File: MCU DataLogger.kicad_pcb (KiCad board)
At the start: 2 copper layers, 29 parts, among them J1 Conn_01x04_Male, J2 Conn_01x04_Male, J3 Conn_01x09_Male, J4 Conn_02x03_Odd_Even, U1 24LC1025, U2 24LC1025, U3 DS1337S+, U4 ATMEGA328P-AU, Y1 32.768 KHz, Y2 16 MHz

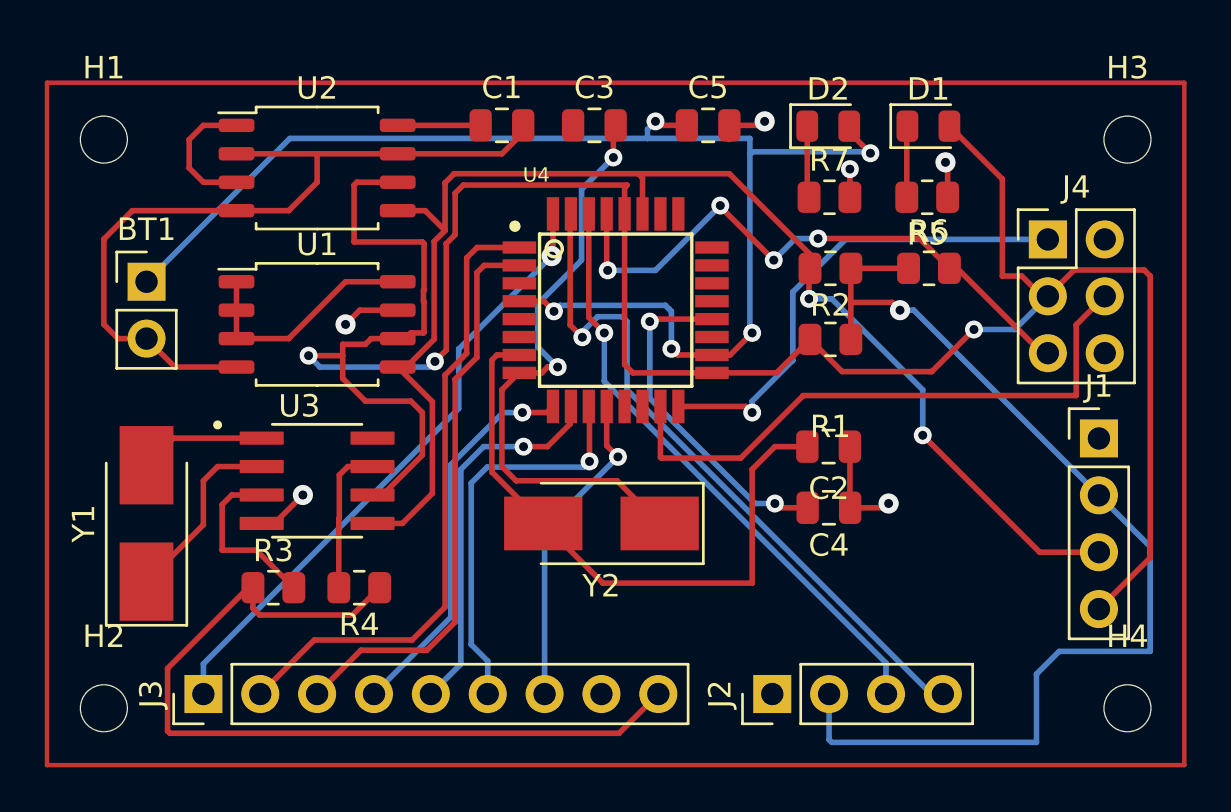
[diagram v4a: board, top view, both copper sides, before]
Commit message: Add Cu surface 1/2
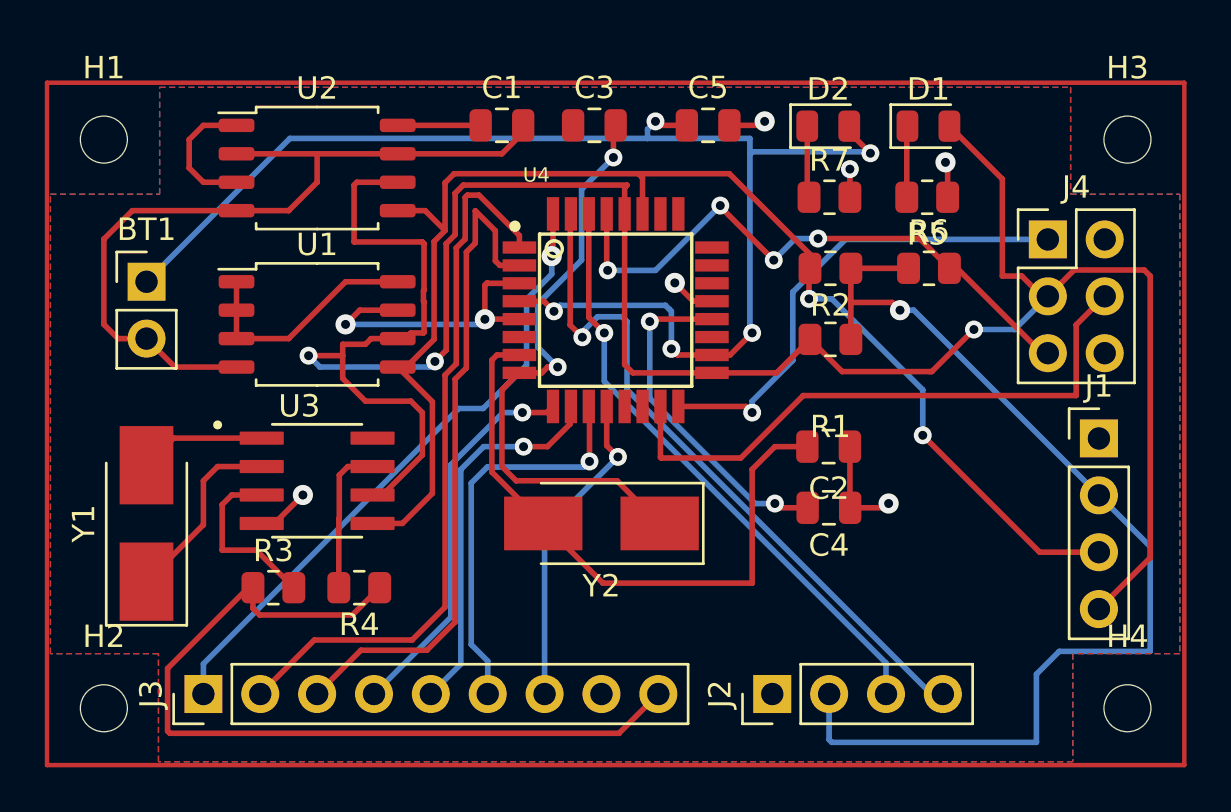
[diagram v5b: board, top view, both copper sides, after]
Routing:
- net GND: track 50.5 -> 62.9 mm, vias 6 -> 8
- net /D4: track 25.5 -> 30.0 mm
- net /D3: track 28.4 -> 32.3 mm
- net /D2: track 27.9 -> 28.6 mm
- added copper zone on F.Cu, net /Vcc
- added copper zone on B.Cu, net GND
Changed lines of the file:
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@@
   (segment (start 75.502 102.806) (end 75.692 102.616) (width 0.25) (layer "F.Cu") (net 2))
   (segment (start 42.545 95.25) (end 43.815 96.52) (width 0.25) (layer "F.Cu") (net 2))
+  (segment (start 57.7596 92.7608) (end 57.7788 92.78) (width 0.25) (layer "F.Cu") (net 2))
+  (segment (start 67.8 93.58) (end 66.9608 93.58) (width 0.25) (layer "F.Cu") (net 2))
   (segment (start 69.977 85.725) (end 70.1548 85.5472) (width 0.25) (layer "F.Cu") (net 2))
-  (segment (start 68.58 85.725) (end 68.58 86.36) (width 0.25) (layer "F.Cu") (net 2))
+  (segment (start 57.6644 94.38) (end 57.658 94.3864) (width 0.25) (layer "F.Cu") (net 2))
   (segment (start 78.3275 87.4715) (end 78.232 87.376) (width 0.25) (layer "F.Cu") (net 2))
   (segment (start 59.37 86.045) (end 58.42 86.995) (width 0.25) (layer "F.Cu") (net 2))
   (segment (start 47.69 103.505) (end 48.26 103.505) (width 0.25) (layer "F.Cu") (net 2))
+  (segment (start 57.658 94.3864) (end 57.658 92.8624) (width 0.25) (layer "F.Cu") (net 2))
   (segment (start 40.64 90.805) (end 41.91 89.535) (width 0.25) (layer "F.Cu") (net 2))
   (segment (start 46.565 86.995) (end 50.165 86.995) (width 0.25) (layer "F.Cu") (net 2))
+  (segment (start 57.658 92.8624) (end 57.7596 92.7608) (width 0.25) (layer "F.Cu") (net 2))
   (segment (start 73.9625 87.6785) (end 73.9625 88.935) (width 0.25) (layer "F.Cu") (net 2))
   (segment (start 46.565 89.535) (end 48.895 89.535) (width 0.25) (layer "F.Cu") (net 2))
@@
   (segment (start 42.545 95.25) (end 41.275 95.25) (width 0.25) (layer "F.Cu") (net 2))
   (segment (start 41.275 95.25) (end 40.64 94.615) (width 0.25) (layer "F.Cu") (net 2))
+  (segment (start 66.9608 93.58) (end 66.1416 92.7608) (width 0.25) (layer "F.Cu") (net 2))
   (segment (start 41.91 89.535) (end 46.565 89.535) (width 0.25) (layer "F.Cu") (net 2))
   (segment (start 68.58 85.725) (end 69.977 85.725) (width 0.25) (layer "F.Cu") (net 2))
@@
   (segment (start 59.37 85.725) (end 59.37 86.045) (width 0.25) (layer "F.Cu") (net 2))
   (segment (start 40.64 94.615) (end 40.64 90.805) (width 0.25) (layer "F.Cu") (net 2))
+  (segment (start 57.7788 92.78) (end 59.2 92.78) (width 0.25) (layer "F.Cu") (net 2))
+  (segment (start 59.2 94.38) (end 57.6644 94.38) (width 0.25) (layer "F.Cu") (net 2))
   (segment (start 52.07 93.98) (end 51.435 94.615) (width 0.25) (layer "F.Cu") (net 2))
   (segment (start 43.815 96.52) (end 46.565 96.52) (width 0.25) (layer "F.Cu") (net 2))
@@
   (via (at 75.692 102.616) (size 0.9) (drill 0.4) (layers "F.Cu" "B.Cu") (net 2))
   (via (at 51.435 94.615) (size 0.9) (drill 0.4) (layers "F.Cu" "B.Cu") (net 2))
+  (via (at 66.1416 92.7608) (size 0.9) (drill 0.4) (layers "F.Cu" "B.Cu") (net 2))
+  (via (at 57.658 94.3864) (size 0.9) (drill 0.4) (layers "F.Cu" "B.Cu") (net 2))
+  (segment (start 57.658 94.3864) (end 57.4294 94.615) (width 0.25) (layer "B.Cu") (net 2))
+  (segment (start 57.4294 94.615) (end 51.435 94.615) (width 0.25) (layer "B.Cu") (net 2))
   (segment (start 60.9092 96.52) (end 60.46 96.52) (width 0.25) (layer "F.Cu") (net 3))
   (segment (start 63.56 101.6) (end 59.055 101.6) (width 0.25) (layer "F.Cu") (net 3))
@@
   (segment (start 60.7 91.507736) (end 60.7 89.68) (width 0.25) (layer "F.Cu") (net 11))
   (via (at 60.6435 91.564236) (size 0.9) (drill 0.4) (layers "F.Cu" "B.Cu") (net 11))
-  (segment (start 60.6435 91.564236) (end 56.4896 95.718136) (width 0.25) (layer "B.Cu") (net 11))
+  (segment (start 60.6435 91.564236) (end 60.6435 92.370194) (width 0.25) (layer "B.Cu") (net 11))
+  (segment (start 57.585616 98.370384) (end 56.4896 98.370384) (width 0.25) (layer "B.Cu") (net 11))
+  (segment (start 56.4896 98.370384) (end 45.085 109.774984) (width 0.25) (layer "B.Cu") (net 11))
+  (segment (start 59.5185 93.495194) (end 59.5185 96.4375) (width 0.25) (layer "B.Cu") (net 11))
+  (segment (start 60.6435 92.370194) (end 59.5185 93.495194) (width 0.25) (layer "B.Cu") (net 11))
   (segment (start 45.085 109.774984) (end 45.085 111.125) (width 0.25) (layer "B.Cu") (net 11))
-  (segment (start 56.4896 95.718136) (end 56.4896 98.370384) (width 0.25) (layer "B.Cu") (net 11))
-  (segment (start 56.4896 98.370384) (end 45.085 109.774984) (width 0.25) (layer "B.Cu") (net 11))
+  (segment (start 59.5185 96.4375) (end 57.585616 98.370384) (width 0.25) (layer "B.Cu") (net 11))
+  (segment (start 56.78 90.796792) (end 56.3808 91.195992) (width 0.25) (layer "F.Cu") (net 12))
+  (segment (start 56.78 88.941196) (end 56.78 90.796792) (width 0.25) (layer "F.Cu") (net 12))
+  (segment (start 57.3968 88.842) (end 56.879196 88.842) (width 0.25) (layer "F.Cu") (net 12))
+  (segment (start 59.2 91.18) (end 59.2 90.6452) (width 0.25) (layer "F.Cu") (net 12))
+  (segment (start 54.4068 108.712) (end 50.038 108.712) (width 0.25) (layer "F.Cu") (net 12))
+  (segment (start 50.038 108.712) (end 47.625 111.125) (width 0.25) (layer "F.Cu") (net 12))
+  (segment (start 56.879196 88.842) (end 56.78 88.941196) (width 0.25) (layer "F.Cu") (net 12))
+  (segment (start 56.3808 91.195992) (end 56.3808 96.3748) (width 0.25) (layer "F.Cu") (net 12))
   (segment (start 55.88 107.2388) (end 54.4068 108.712) (width 0.25) (layer "F.Cu") (net 12))
-  (segment (start 50.038 108.712) (end 47.625 111.125) (width 0.25) (layer "F.Cu") (net 12))
-  (segment (start 54.4068 108.712) (end 50.038 108.712) (width 0.25) (layer "F.Cu") (net 12))
-  (segment (start 59.2 91.18) (end 57.3084 91.18) (width 0.25) (layer "F.Cu") (net 12))
-  (segment (start 56.8452 95.9104) (end 55.88 96.8756) (width 0.25) (layer "F.Cu") (net 12))
   (segment (start 55.88 96.8756) (end 55.88 107.2388) (width 0.25) (layer "F.Cu") (net 12))
-  (segment (start 56.8452 91.6432) (end 56.8452 95.9104) (width 0.25) (layer "F.Cu") (net 12))
-  (segment (start 57.3084 91.18) (end 56.8452 91.6432) (width 0.25) (layer "F.Cu") (net 12))
+  (segment (start 59.2 90.6452) (end 57.3968 88.842) (width 0.25) (layer "F.Cu") (net 12))
+  (segment (start 56.3808 96.3748) (end 55.88 96.8756) (width 0.25) (layer "F.Cu") (net 12))
+  (segment (start 57.23 89.5388) (end 58.125 90.4338) (width 0.25) (layer "F.Cu") (net 13))
+  (segment (start 58.125 91.78) (end 58.325 91.98) (width 0.25) (layer "F.Cu") (net 13))
+  (segment (start 56.33 107.9064) (end 56.33 97.061996) (width 0.25) (layer "F.Cu") (net 13))
   (segment (start 52.1208 109.1692) (end 55.0672 109.1692) (width 0.25) (layer "F.Cu") (net 13))
   (segment (start 55.0672 109.1692) (end 56.33 107.9064) (width 0.25) (layer "F.Cu") (net 13))
-  (segment (start 57.3024 92.3036) (end 57.626 91.98) (width 0.25) (layer "F.Cu") (net 13))
-  (segment (start 56.33 107.9064) (end 56.33 97.061996) (width 0.25) (layer "F.Cu") (net 13))
-  (segment (start 57.626 91.98) (end 59.2 91.98) (width 0.25) (layer "F.Cu") (net 13))
-  (segment (start 56.33 97.061996) (end 57.3024 96.089596) (width 0.25) (layer "F.Cu") (net 13))
+  (segment (start 57.23 90.983188) (end 57.23 89.5388) (width 0.25) (layer "F.Cu") (net 13))
+  (segment (start 56.33 97.061996) (end 56.8308 96.561196) (width 0.25) (layer "F.Cu") (net 13))
+  (segment (start 56.8308 96.561196) (end 56.8308 91.382388) (width 0.25) (layer "F.Cu") (net 13))
+  (segment (start 58.125 90.4338) (end 58.125 91.78) (width 0.25) (layer "F.Cu") (net 13))
+  (segment (start 58.325 91.98) (end 59.2 91.98) (width 0.25) (layer "F.Cu") (net 13))
   (segment (start 50.165 111.125) (end 52.1208 109.1692) (width 0.25) (layer "F.Cu") (net 13))
-  (segment (start 57.3024 96.089596) (end 57.3024 92.3036) (width 0.25) (layer "F.Cu") (net 13))
+  (segment (start 56.8308 91.382388) (end 57.23 90.983188) (width 0.25) (layer "F.Cu") (net 13))
   (segment (start 59.3344 98.552) (end 60.428 98.552) (width 0.25) (layer "F.Cu") (net 14))
   (segment (start 60.428 98.552) (end 60.7 98.28) (width 0.25) (layer "F.Cu") (net 14))
@@
   (segment (start 70.612 102.616) (end 69.724396 102.616) (width 0.25) (layer "B.Cu") (net 35))
   (segment (start 65.024 97.915604) (end 65.024 94.488) (width 0.25) (layer "B.Cu") (net 35))
+  (zone (net 7) (net_name "/Vcc") (layer "F.Cu") (hatch edge 0.508)
+    (connect_pads (clearance 0.508))
+    (min_thickness 0.254) (filled_areas_thickness no)
+    (fill yes (mode hatch) (thermal_gap 0.508) (thermal_bridge_width 0.508)
+      (hatch_thickness 1.016) (hatch_gap 1.524) (hatch_orientation 0)
+      (hatch_border_algorithm hatch_thickness) (hatch_min_hole_area 0.3))
+    (polygon
+      (pts
+        (xy 83.82 88.7984)
+        (xy 88.6968 88.7984)
+        (xy 88.6968 109.3216)
+        (xy 83.9216 109.3216)
+        (xy 83.9216 114.1476)
+        (xy 43.0784 114.1476)
+        (xy 43.0784 109.3216)
+        (xy 38.2524 109.3216)
+        (xy 38.2524 88.7984)
+        (xy 43.1292 88.7984)
+        (xy 43.1292 84.0232)
+        (xy 83.82 84.0232)
+      )
+    )
+  )
+  (zone (net 2) (net_name "GND") (layer "B.Cu") (hatch edge 0.508)
+    (connect_pads (clearance 0.508))
+    (min_thickness 0.254) (filled_areas_thickness no)
+    (fill yes (mode hatch) (thermal_gap 0.508) (thermal_bridge_width 0.508)
+      (hatch_thickness 1.016) (hatch_gap 1.524) (hatch_orientation 0)
+      (hatch_border_algorithm hatch_thickness) (hatch_min_hole_area 0.3))
+    (polygon
+      (pts
+        (xy 83.82 88.7984)
+        (xy 88.6968 88.7984)
+        (xy 88.6968 109.3216)
+        (xy 83.9216 109.3216)
+        (xy 83.9216 114.1476)
+        (xy 43.0784 114.1476)
+        (xy 43.0784 109.3216)
+        (xy 38.2524 109.3216)
+        (xy 38.2524 88.7984)
+        (xy 43.1292 88.7984)
+        (xy 43.1292 84.0232)
+        (xy 83.82 84.0232)
+      )
+    )
+  )
 )

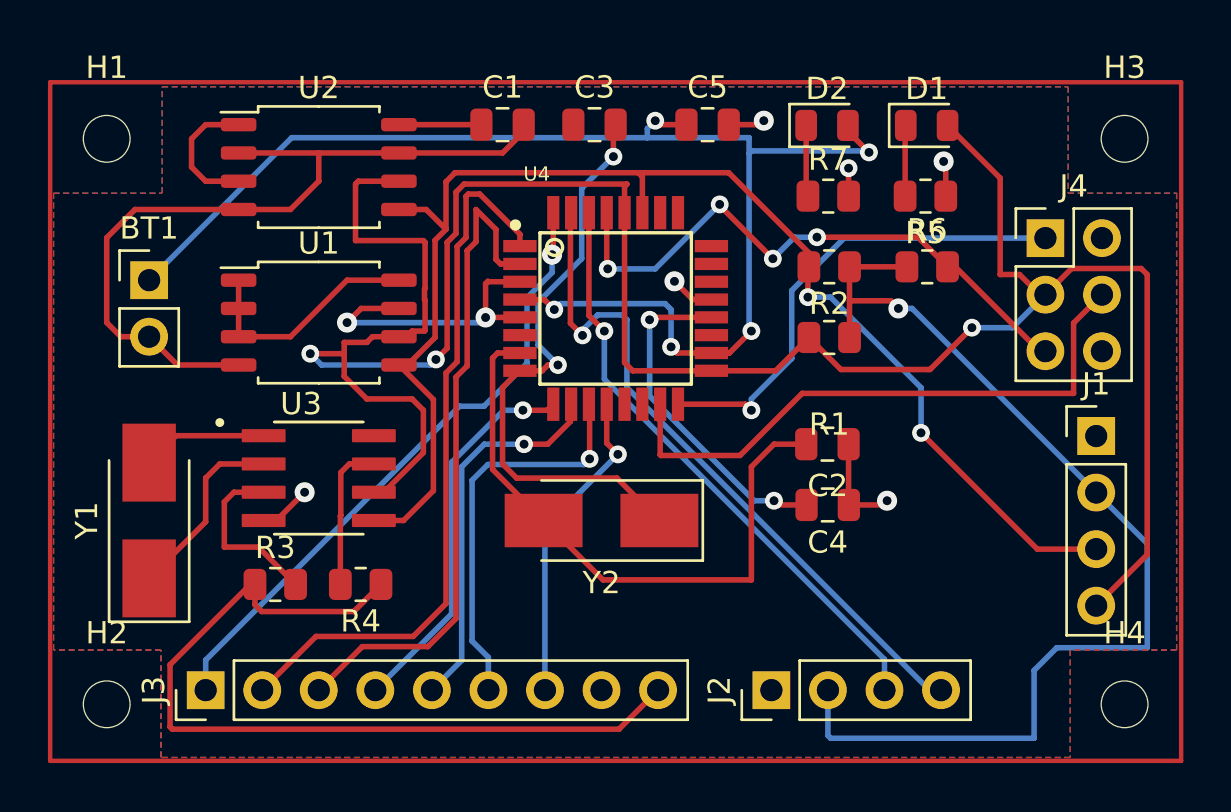
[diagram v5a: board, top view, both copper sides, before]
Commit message: Completed routing
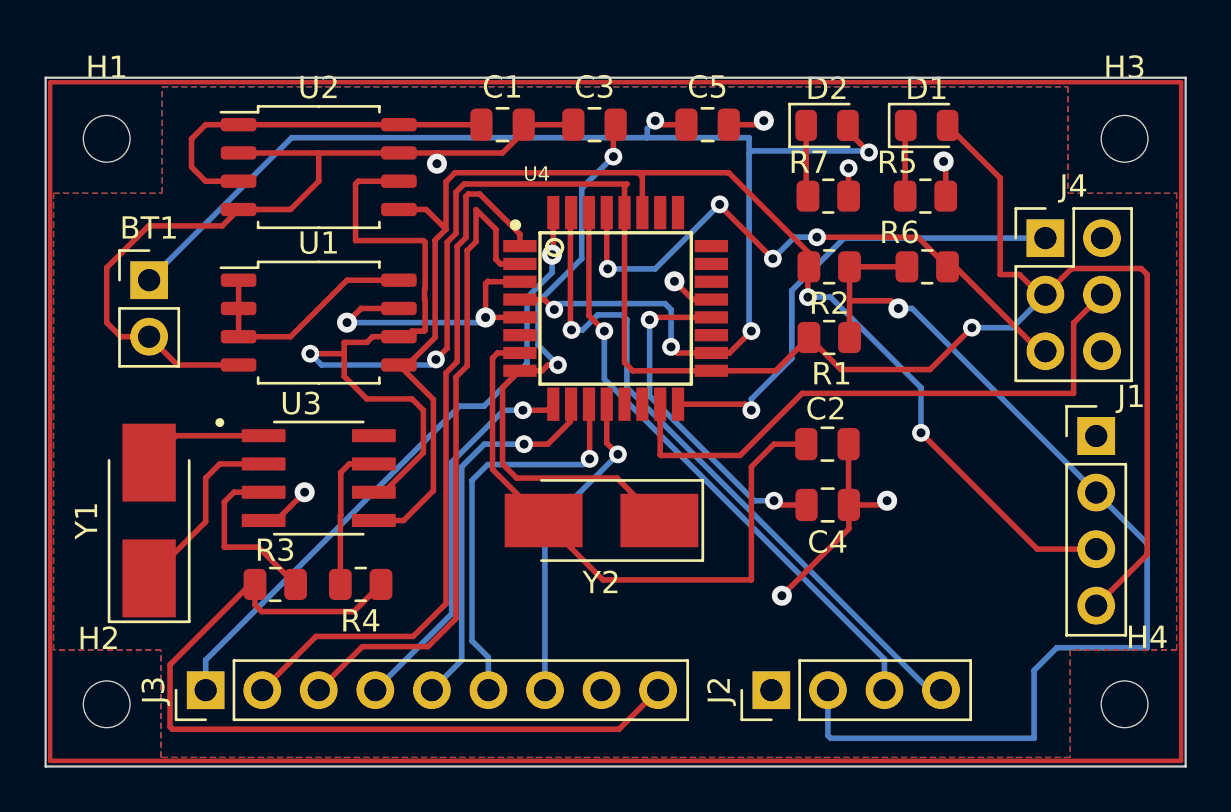
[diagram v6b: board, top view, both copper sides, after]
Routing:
- net GND: track 62.9 -> 70.1 mm, vias 8 -> 10
- net /Vcc: track 106.7 -> 113.9 mm
- net Net-(U3-Pad2): track 8.98 -> 8.43 mm
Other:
- board outline added: 51.2 x 30.9 mm

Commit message: Add silkscreen
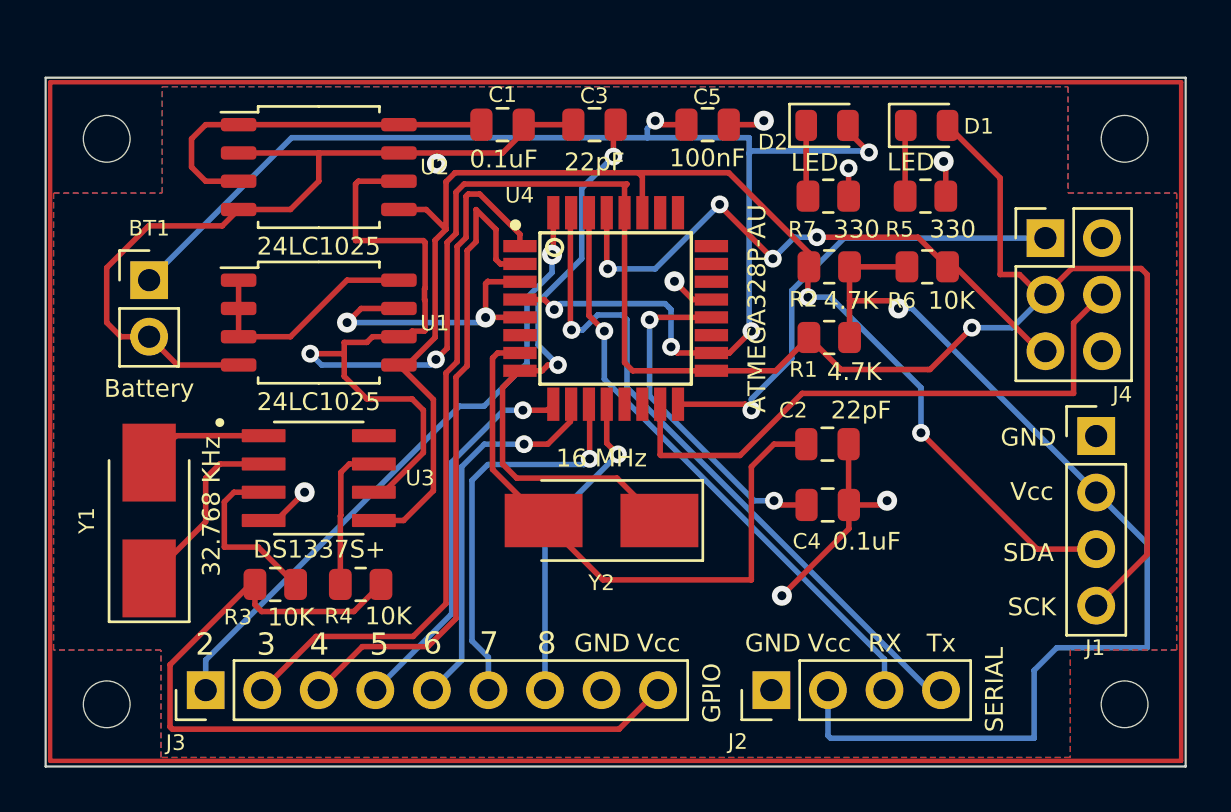
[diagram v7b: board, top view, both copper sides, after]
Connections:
- BT1 pad 1: Net-(BT1-Pad1) -> /Vcc
- C5 pad 1: Net-(BT1-Pad1) -> /Vcc
- D2 pad 2: Net-(BT1-Pad1) -> /Vcc
- U4 pad 18: Net-(BT1-Pad1) -> /Vcc
- U4 pad 4: Net-(BT1-Pad1) -> /Vcc
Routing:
- net Net-(BT1-Pad1): track 60.8 -> 0.00 mm, vias 5 -> 0
- net /Vcc: track 113.9 -> 174.7 mm, vias 1 -> 6
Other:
- board text added: "2"
- board text added: "3"
- board text added: "4"
- board text added: "5"
- board text added: "6"
- board text added: "7"
- board text added: "8"
- board text added: "GND"
- board text added: "GPIO"
- board text added: "RX"
- board text added: "SCK"
- board text added: "SDA"
- board text added: "SERIAL"
- board text added: "Tx"
- board text added: "Vcc"
